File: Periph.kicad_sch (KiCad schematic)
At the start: 9 parts, among them U8 W25Q128JVS, U9 ICM-42688-P

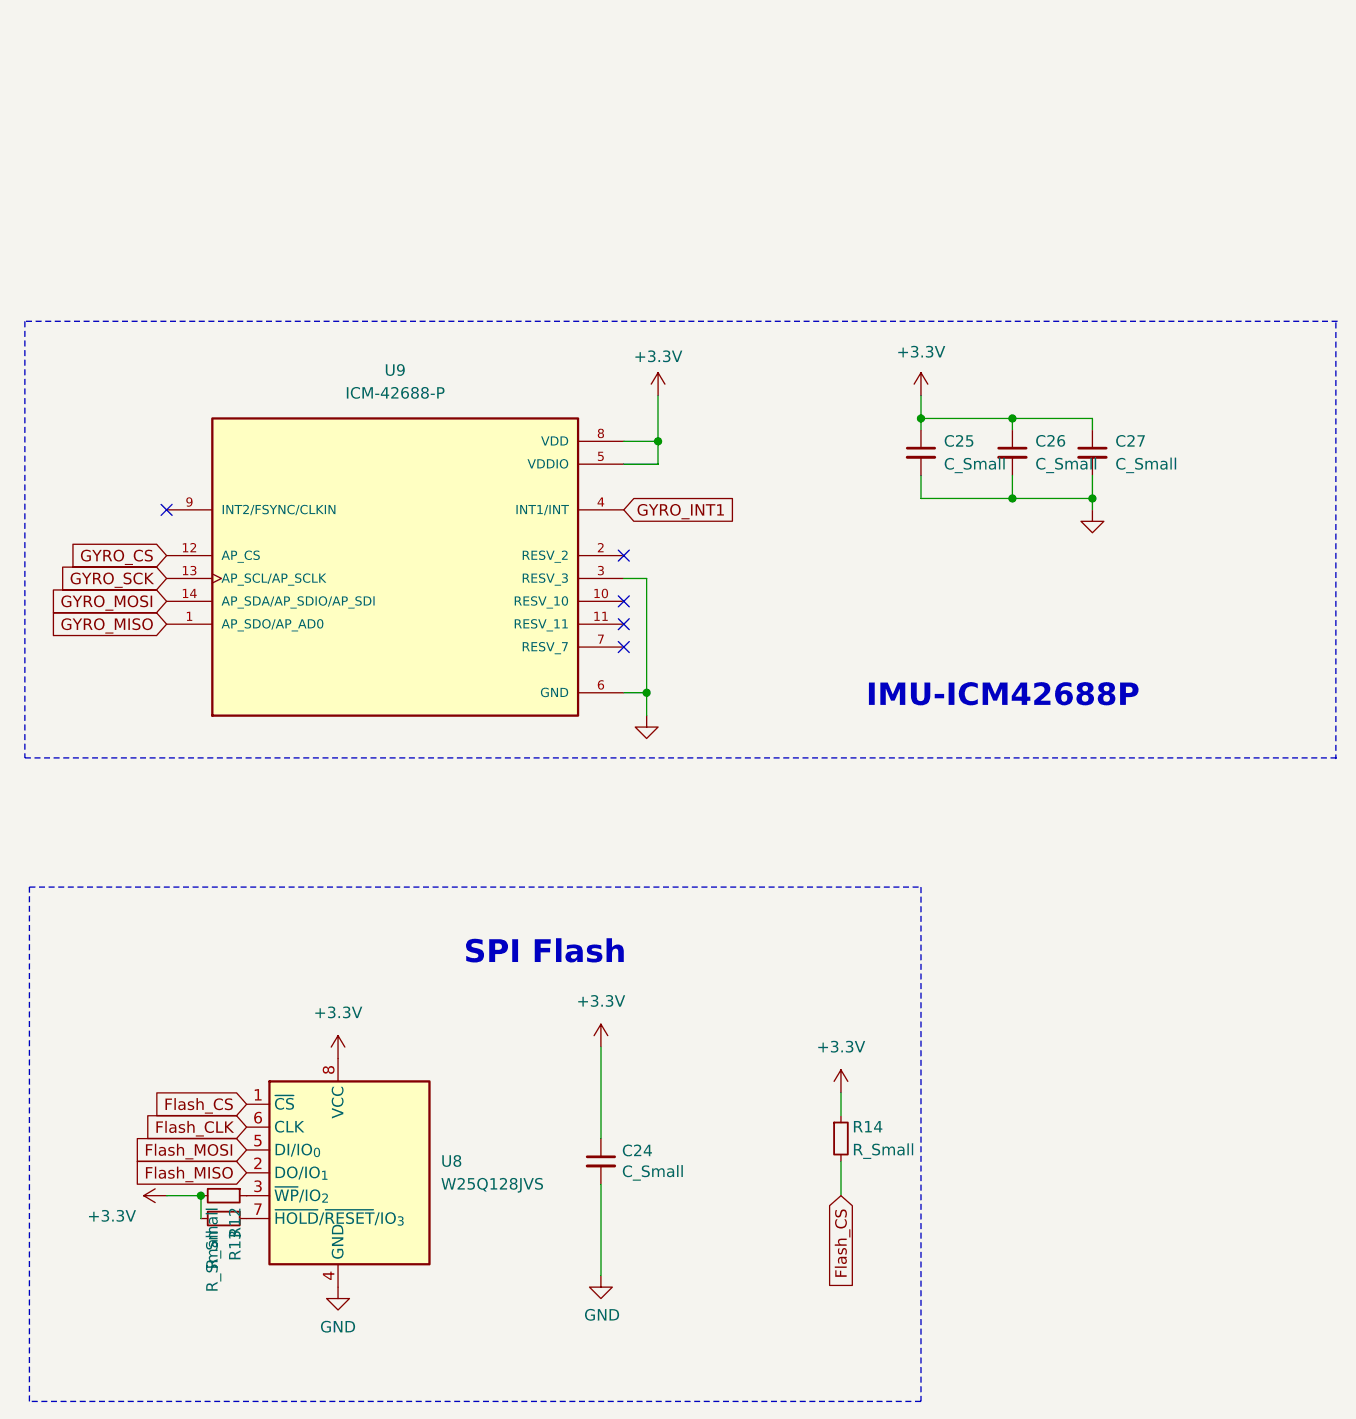
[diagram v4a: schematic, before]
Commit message: update value for capacity and  resistor
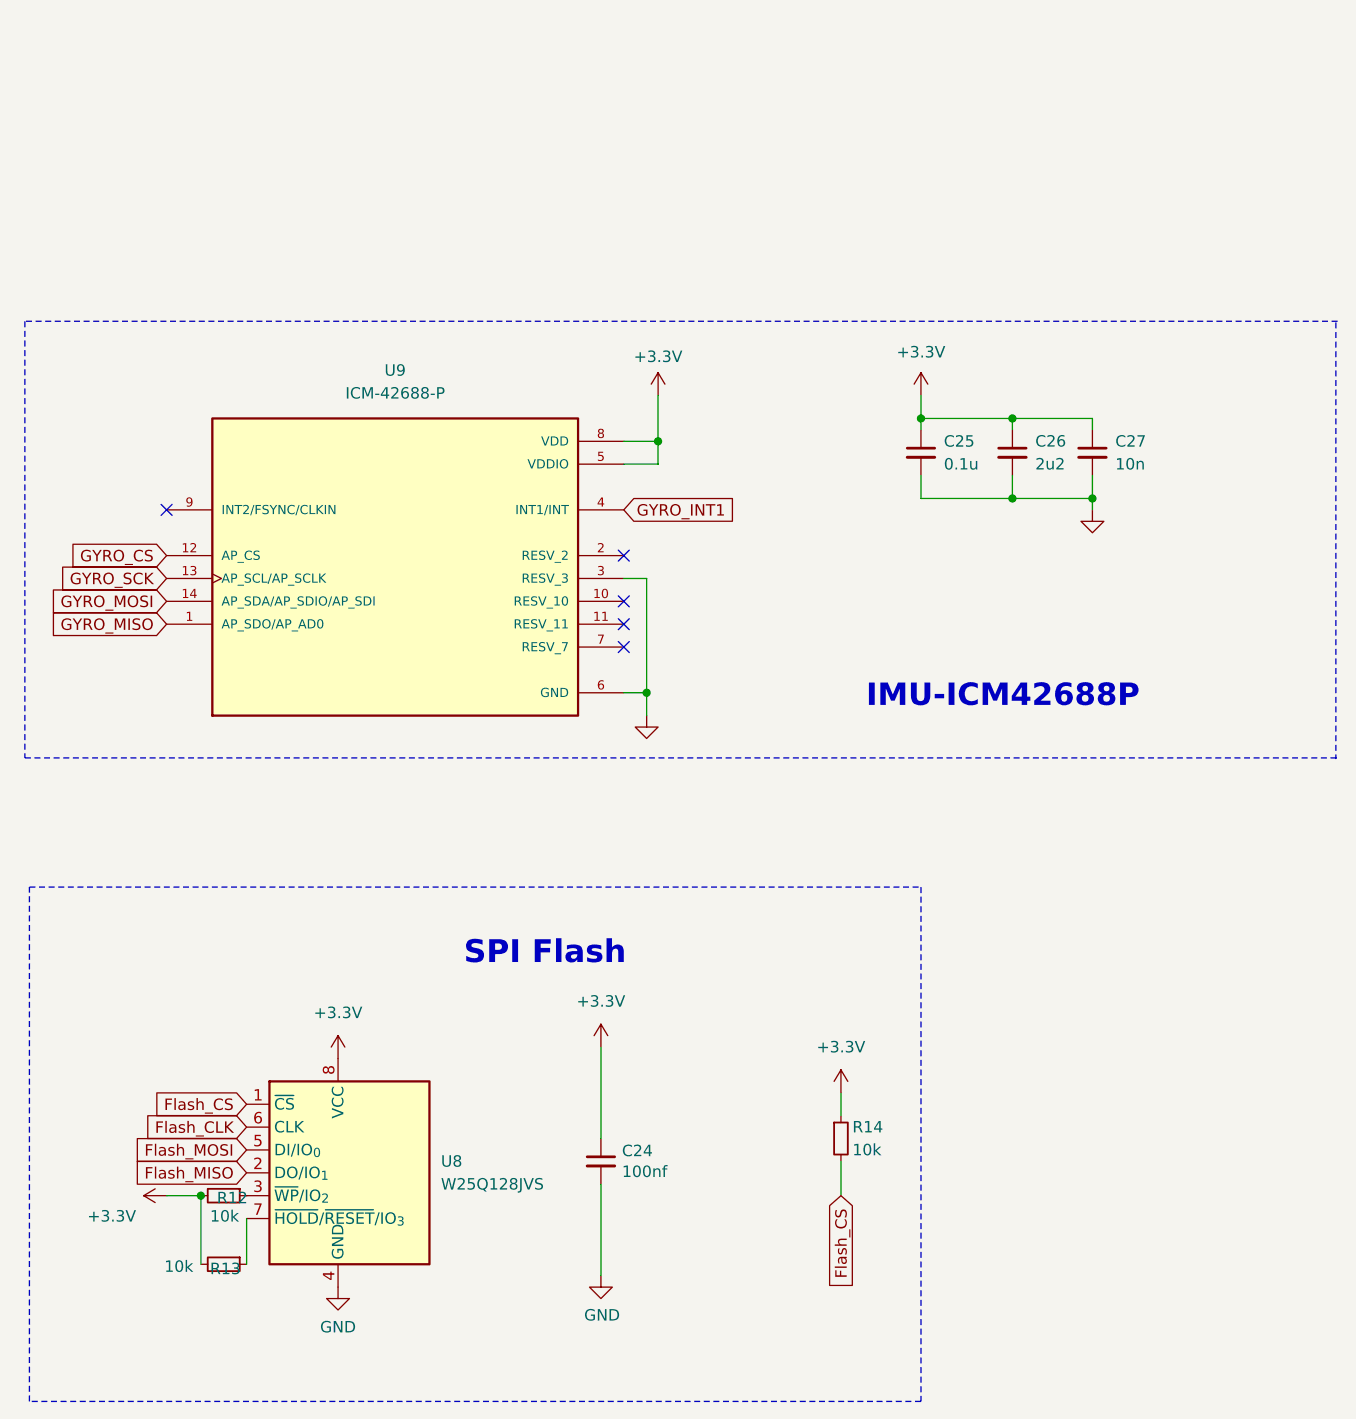
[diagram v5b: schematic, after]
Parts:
- C24: value C_Small -> 100nf
- C25: value C_Small -> 0.1u
- C26: value C_Small -> 2u2
- C27: value C_Small -> 10n
- R12, R13, R14: value R_Small -> 10k
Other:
- moved on the sheet: R13
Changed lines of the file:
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@@
 	(wire
 		(pts
-			(xy 63.5 152.4) (xy 63.5 149.86)
+			(xy 63.5 157.48) (xy 63.5 149.86)
 		)
 		(stroke
@@
 		(pts
 			(xy 134.62 146.05) (xy 134.62 149.86)
+		)
+		(stroke
+			(width 0)
+			(type default)
+		)
+	)
+	(wire
+		(pts
+			(xy 68.58 157.48) (xy 68.58 152.4)
 		)
 		(stroke
@@
 		(dnp no)
 		(property "Reference" "R12"
-			(at 67.31 151.13 0)
+			(at 65.278 150.114 90)
 			(effects
 				(font
@@
 			)
 		)
-		(property "Value" "R_Small"
-			(at 64.77 151.13 0)
+		(property "Value" "10k"
+			(at 64.516 152.146 90)
 			(effects
 				(font
@@
 			)
 		)
-		(property "Value" "C_Small"
+		(property "Value" "100nf"
 			(at 110.2868 147.193 0)
 			(effects
@@
 			)
 		)
-		(property "Value" "C_Small"
+		(property "Value" "2u2"
 			(at 156.21 68.58 0)
 			(effects
@@
 			)
 		)
-		(property "Value" "C_Small"
+		(property "Value" "0.1u"
 			(at 146.05 68.5862 0)
 			(effects
@@
 			)
 		)
-		(property "Value" "R_Small"
+		(property "Value" "10k"
 			(at 135.89 144.78 0)
 			(effects
@@
 	(symbol
 		(lib_id "Device:R_Small")
-		(at 66.04 152.4 270)
+		(at 66.04 157.48 270)
 		(unit 1)
 		(exclude_from_sim no)
@@
 		(dnp no)
 		(property "Reference" "R13"
-			(at 67.31 153.67 0)
+			(at 64.516 157.988 90)
 			(effects
 				(font
@@
 			)
 		)
-		(property "Value" "R_Small"
-			(at 64.77 153.67 0)
+		(property "Value" "10k"
+			(at 59.436 157.734 90)
 			(effects
 				(font
@@
 		)
 		(property "Footprint" "Resistor_SMD:R_0402_1005Metric"
-			(at 66.04 152.4 0)
+			(at 66.04 157.48 0)
 			(effects
 				(font
@@
 		)
 		(property "Datasheet" "~"
-			(at 66.04 152.4 0)
+			(at 66.04 157.48 0)
 			(effects
 				(font
@@
 		)
 		(property "Description" ""
-			(at 66.04 152.4 0)
+			(at 66.04 157.48 0)
 			(effects
 				(font
@@
 		)
 		(property "LCSC Part #" "C25744"
-			(at 66.04 152.4 0)
+			(at 66.04 157.48 0)
 			(effects
 				(font
@@
 			)
 		)
-		(property "Value" "C_Small"
+		(property "Value" "10n"
 			(at 165.1 68.5862 0)
 			(effects

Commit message: save
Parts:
- renumbered C24 to C23, C25 to C24, C26 to C25, C27 to C26, R12 to R11, R13 to R12, R14 to R13, U9 to U10, U8 to U9
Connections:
- net GYRO_INT2: now reaches U10.9 (INT2/FSYNC/CLKIN)
- net Flash_CLK renamed Flash_SCK
- no-connect marks 5 -> 4
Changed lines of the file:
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@@
-	)
-	(no_connect
-		(at 59.69 73.66)
 	)
 	(no_connect
@@
 	(polyline
 		(pts
-			(xy 44.069 52.705) (xy 189.865 52.705)
+			(xy 43.434 53.34) (xy 189.23 53.34)
 		)
 		(stroke
@@
 		)
 	)
-	(global_label "Flash_CLK"
+	(global_label "Flash_SCK"
 		(shape input)
 		(at 68.58 142.24 180)
@@
 		)
 		(property "Intersheetrefs" "${INTERSHEET_REFS}"
-			(at 56.5512 142.1606 0)
+			(at 55.7978 142.24 0)
 			(effects
 				(font
@@
 				)
 				(justify left)
+				(hide yes)
+			)
+		)
+	)
+	(global_label "GYRO_INT2"
+		(shape input)
+		(at 59.69 73.66 180)
+		(effects
+			(font
+				(size 1.27 1.27)
+			)
+			(justify right)
+		)
+		(property "Intersheetrefs" "${INTERSHEET_REFS}"
+			(at 59.69 73.66 0)
+			(effects
+				(font
+					(size 1.27 1.27)
+				)
 				(hide yes)
 			)
@@
 		(on_board yes)
 		(dnp no)
-		(property "Reference" "R12"
+		(property "Reference" "R11"
 			(at 65.278 150.114 90)
 			(effects
@@
 			(project "MX_IMU"
 				(path "/8ed38441-7d4e-4e89-870f-07e11c6dce38/57f4b5bf-da86-4b65-9b05-7c9ef99c472c"
-					(reference "R12")
+					(reference "R11")
 					(unit 1)
 				)
@@
 		(on_board yes)
 		(dnp no)
-		(property "Reference" "#PWR060"
+		(property "Reference" "#PWR063"
 			(at 63.5 149.86 0)
 			(effects
@@
 			(project "MX_IMU"
 				(path "/8ed38441-7d4e-4e89-870f-07e11c6dce38/57f4b5bf-da86-4b65-9b05-7c9ef99c472c"
-					(reference "#PWR060")
+					(reference "#PWR063")
 					(unit 1)
 				)
@@
 		(dnp no)
 		(fields_autoplaced yes)
-		(property "Reference" "#PWR068"
+		(property "Reference" "#PWR071"
 			(at 143.51 64.77 0)
 			(effects
@@
 			(project "MX_IMU"
 				(path "/8ed38441-7d4e-4e89-870f-07e11c6dce38/57f4b5bf-da86-4b65-9b05-7c9ef99c472c"
-					(reference "#PWR068")
+					(reference "#PWR071")
 					(unit 1)
 				)
@@
 		(dnp no)
 		(fields_autoplaced yes)
-		(property "Reference" "#PWR063"
+		(property "Reference" "#PWR066"
 			(at 107.95 137.16 0)
 			(effects
@@
 			(project ""
 				(path "/8ed38441-7d4e-4e89-870f-07e11c6dce38/57f4b5bf-da86-4b65-9b05-7c9ef99c472c"
-					(reference "#PWR063")
+					(reference "#PWR066")
 					(unit 1)
 				)
@@
 		(dnp no)
 		(fields_autoplaced yes)
-		(property "Reference" "#PWR065"
+		(property "Reference" "#PWR068"
 			(at 113.03 102.87 0)
 			(effects
@@
 			(project "MX_IMU"
 				(path "/8ed38441-7d4e-4e89-870f-07e11c6dce38/57f4b5bf-da86-4b65-9b05-7c9ef99c472c"
-					(reference "#PWR065")
+					(reference "#PWR068")
 					(unit 1)
 				)
@@
 		(on_board yes)
 		(dnp no)
-		(property "Reference" "C24"
+		(property "Reference" "C23"
 			(at 110.2868 144.8816 0)
 			(effects
@@
 			(project "MX_IMU"
 				(path "/8ed38441-7d4e-4e89-870f-07e11c6dce38/57f4b5bf-da86-4b65-9b05-7c9ef99c472c"
-					(reference "C24")
+					(reference "C23")
 					(unit 1)
 				)
@@
 		(on_board yes)
 		(dnp no)
-		(property "Reference" "#PWR064"
+		(property "Reference" "#PWR067"
 			(at 107.95 165.1 0)
 			(effects
@@
 			(project "MX_IMU"
 				(path "/8ed38441-7d4e-4e89-870f-07e11c6dce38/57f4b5bf-da86-4b65-9b05-7c9ef99c472c"
-					(reference "#PWR064")
+					(reference "#PWR067")
 					(unit 1)
 				)
@@
 		(on_board yes)
 		(dnp no)
-		(property "Reference" "C26"
+		(property "Reference" "C25"
 			(at 156.21 66.04 0)
 			(effects
@@
 			(project "MX_IMU"
 				(path "/8ed38441-7d4e-4e89-870f-07e11c6dce38/57f4b5bf-da86-4b65-9b05-7c9ef99c472c"
-					(reference "C26")
+					(reference "C25")
 					(unit 1)
 				)
@@
 		(dnp no)
 		(fields_autoplaced yes)
-		(property "Reference" "C25"
+		(property "Reference" "C24"
 			(at 146.05 66.0462 0)
 			(effects
@@
 			(project "MX_IMU"
 				(path "/8ed38441-7d4e-4e89-870f-07e11c6dce38/57f4b5bf-da86-4b65-9b05-7c9ef99c472c"
-					(reference "C25")
+					(reference "C24")
 					(unit 1)
 				)
@@
 		(on_board yes)
 		(dnp no)
-		(property "Reference" "R14"
+		(property "Reference" "R13"
 			(at 135.89 142.24 0)
 			(effects
@@
 			(project "MX_IMU"
 				(path "/8ed38441-7d4e-4e89-870f-07e11c6dce38/57f4b5bf-da86-4b65-9b05-7c9ef99c472c"
-					(reference "R14")
+					(reference "R13")
 					(unit 1)
 				)
@@
 		(dnp no)
 		(fields_autoplaced yes)
-		(property "Reference" "#PWR069"
+		(property "Reference" "#PWR072"
 			(at 162.56 80.01 0)
 			(effects
@@
 			(project "MX_IMU"
 				(path "/8ed38441-7d4e-4e89-870f-07e11c6dce38/57f4b5bf-da86-4b65-9b05-7c9ef99c472c"
-					(reference "#PWR069")
+					(reference "#PWR072")
 					(unit 1)
 				)
@@
 		(dnp no)
 		(fields_autoplaced yes)
-		(property "Reference" "#PWR062"
+		(property "Reference" "#PWR065"
 			(at 78.74 166.37 0)
 			(effects
@@
 			(project "MX_IMU"
 				(path "/8ed38441-7d4e-4e89-870f-07e11c6dce38/57f4b5bf-da86-4b65-9b05-7c9ef99c472c"
-					(reference "#PWR062")
+					(reference "#PWR065")
 					(unit 1)
 				)
@@
 		(dnp no)
 		(fields_autoplaced yes)
-		(property "Reference" "#PWR067"
+		(property "Reference" "#PWR070"
 			(at 134.62 142.24 0)
 			(effects
@@
 			(project ""
 				(path "/8ed38441-7d4e-4e89-870f-07e11c6dce38/57f4b5bf-da86-4b65-9b05-7c9ef99c472c"
-					(reference "#PWR067")
+					(reference "#PWR070")
 					(unit 1)
 				)
@@
 		(on_board yes)
 		(dnp no)
-		(property "Reference" "R13"
+		(property "Reference" "R12"
 			(at 64.516 157.988 90)
 			(effects
@@
 			(project "MX_IMU"
 				(path "/8ed38441-7d4e-4e89-870f-07e11c6dce38/57f4b5bf-da86-4b65-9b05-7c9ef99c472c"
-					(reference "R13")
+					(reference "R12")
 					(unit 1)
 				)
@@
 		(dnp no)
 		(fields_autoplaced yes)
-		(property "Reference" "#PWR066"
+		(property "Reference" "#PWR069"
 			(at 114.3 64.77 0)
 			(effects
@@
 			(project "MX_IMU"
 				(path "/8ed38441-7d4e-4e89-870f-07e11c6dce38/57f4b5bf-da86-4b65-9b05-7c9ef99c472c"
-					(reference "#PWR066")
+					(reference "#PWR069")
 					(unit 1)
 				)
@@
 		(dnp no)
 		(fields_autoplaced yes)
-		(property "Reference" "U9"
+		(property "Reference" "U10"
 			(at 85.09 58.166 0)
 			(effects
@@
 			(project "MX_IMU"
 				(path "/8ed38441-7d4e-4e89-870f-07e11c6dce38/57f4b5bf-da86-4b65-9b05-7c9ef99c472c"
-					(reference "U9")
+					(reference "U10")
 					(unit 1)
 				)
@@
 		(dnp no)
 		(fields_autoplaced yes)
-		(property "Reference" "U8"
+		(property "Reference" "U9"
 			(at 90.17 146.0499 0)
 			(effects
@@
 			(project ""
 				(path "/8ed38441-7d4e-4e89-870f-07e11c6dce38/57f4b5bf-da86-4b65-9b05-7c9ef99c472c"
-					(reference "U8")
+					(reference "U9")
 					(unit 1)
 				)
@@
 		(dnp no)
 		(fields_autoplaced yes)
-		(property "Reference" "C27"
+		(property "Reference" "C26"
 			(at 165.1 66.0462 0)
 			(effects
@@
 			(project "MX_IMU"
 				(path "/8ed38441-7d4e-4e89-870f-07e11c6dce38/57f4b5bf-da86-4b65-9b05-7c9ef99c472c"
-					(reference "C27")
+					(reference "C26")
 					(unit 1)
 				)
@@
 		(dnp no)
 		(fields_autoplaced yes)
-		(property "Reference" "#PWR061"
+		(property "Reference" "#PWR064"
 			(at 78.74 138.43 0)
 			(effects
@@
 			(project "MX_IMU"
 				(path "/8ed38441-7d4e-4e89-870f-07e11c6dce38/57f4b5bf-da86-4b65-9b05-7c9ef99c472c"
-					(reference "#PWR061")
+					(reference "#PWR064")
 					(unit 1)
 				)

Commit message: update
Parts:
- added C23: 0.01u, Capacitor_SMD:C_0402_1005Metric, symbol Device:C_Small
- added LSE: ASEK-32.768KHZ-L-R-T, mylib:XTAL_ASEK-32.768KHZ-L-R-T, symbol ASEK-32.768KHZ-L-R-T:ASEK-32.768KHZ-L-R-T
- renumbered C23 to C24, C24 to C25, C25 to C26, C26 to C27
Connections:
- net +3.3V: now also C23.1, LSE.4 (VDD)
- net GND: now also C23.2, LSE.2 (GND/CASE)
- net GYRO_INT2: no longer names the net of U10.9 (INT2/FSYNC/CLKIN)
- net GYRO_INT2: now also LSE.3 (OUTPUT)
- new net GYRO_LSE: LSE.1 (TRI-STATE)

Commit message: update
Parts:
- renumbered LSE to LSE1
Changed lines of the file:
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@@
 		(dnp no)
 		(fields_autoplaced yes)
-		(property "Reference" "LSE"
+		(property "Reference" "LSE1"
 			(at 109.22 20.32 0)
 			(effects
@@
 			(project ""
 				(path "/8ed38441-7d4e-4e89-870f-07e11c6dce38/57f4b5bf-da86-4b65-9b05-7c9ef99c472c"
-					(reference "LSE")
+					(reference "LSE1")
 					(unit 1)
 				)
